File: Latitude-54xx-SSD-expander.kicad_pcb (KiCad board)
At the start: 4 copper layers, 60 x 112 mm, 24 parts, among them J1 Bus_M.2_Socket_M, J2 Bus_M.2_Socket_M, J3 Bus_M.2_Socket_M, J4 qwiic, U1 clockbuffer_9ZXL0651AKLF

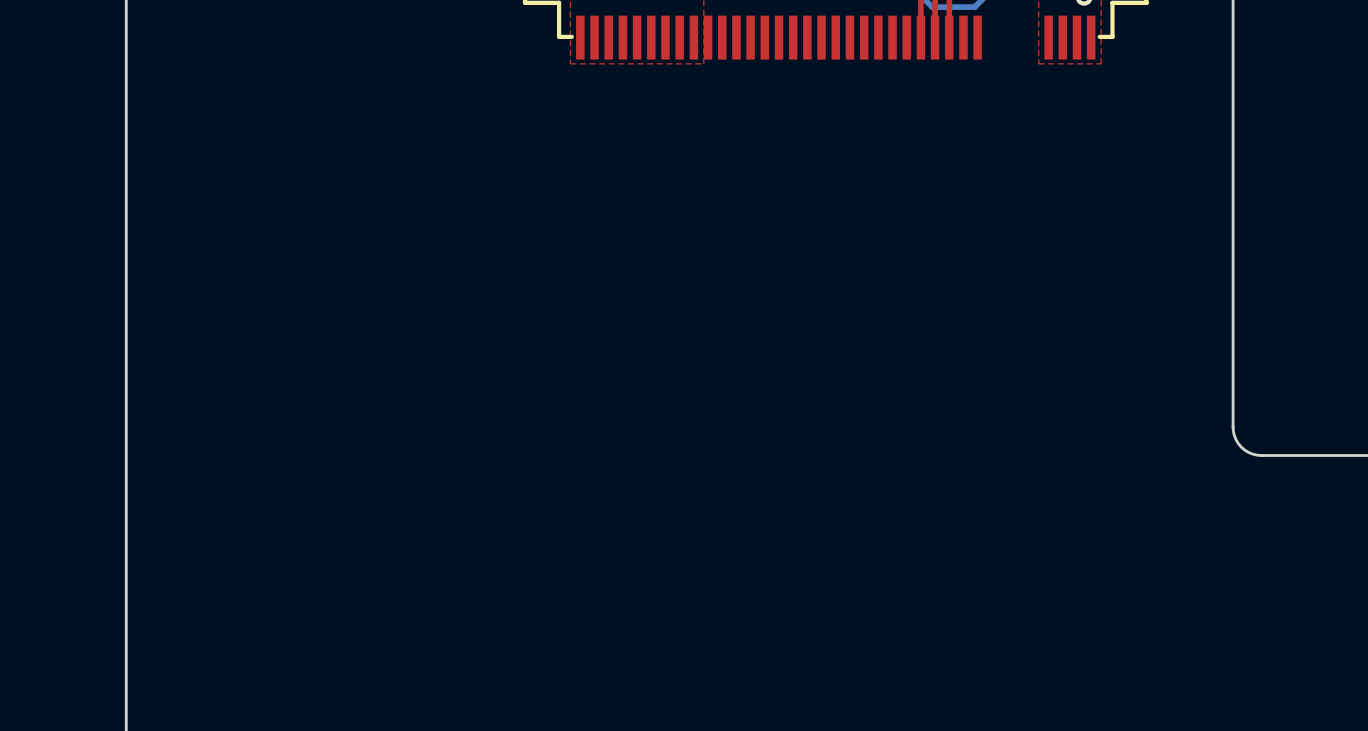
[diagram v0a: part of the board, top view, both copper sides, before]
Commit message: logo concept on the silkscreen
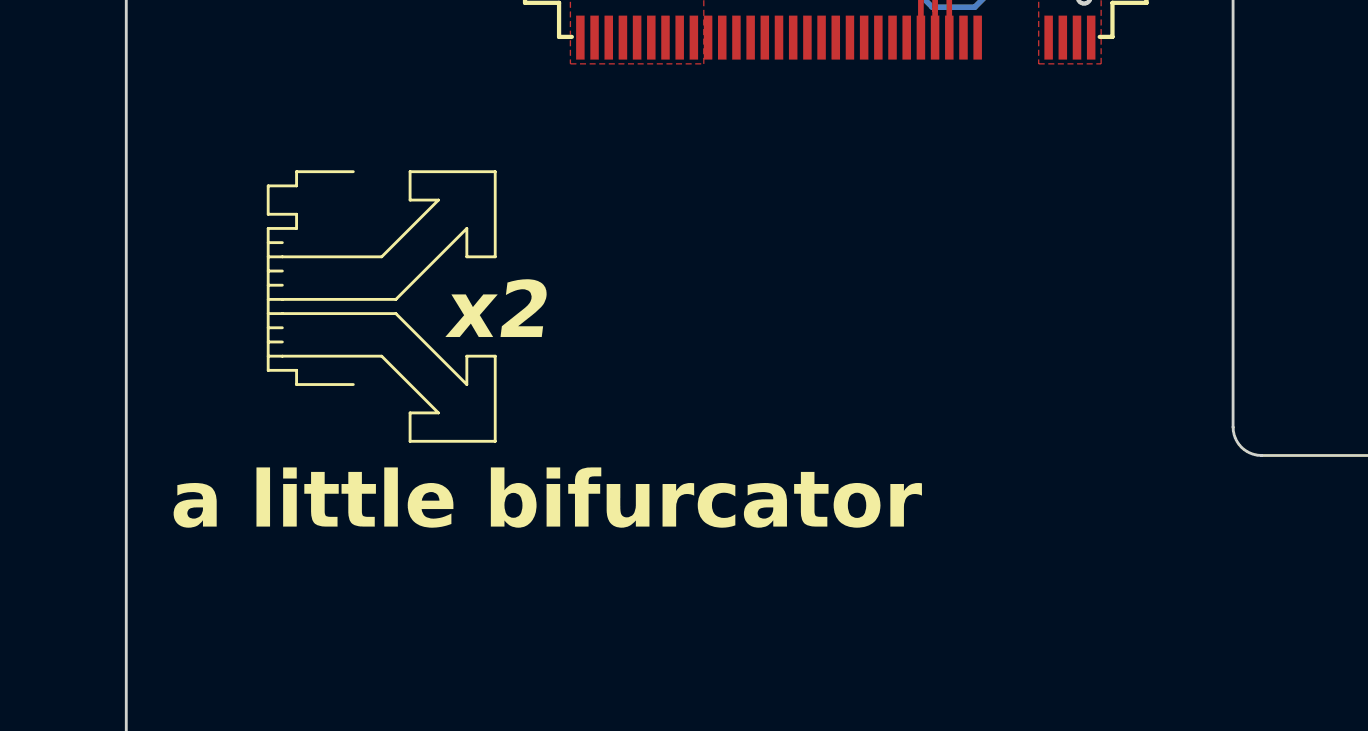
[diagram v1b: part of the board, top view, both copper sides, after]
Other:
- board text added: "a little bifurcator"
- board text added: "x2"

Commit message: Silkscreen adjustments
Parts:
- added G***: LOGO, A-my-stuff:stars, F.Cu at (87.1, 141.1)
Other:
- board text added: "5491 edition"
- board text added: "Buffer SMBus"

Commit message: Added todo list
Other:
- board text added: "TODO: [ ] Properly look into the mounting method to the chassis [ ] Cut off unused PCB area near the end [ ] Come up with a better name/logo"
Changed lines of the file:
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@@
+		)
+	)
+	(gr_text "TODO:\n[ ] Properly look into the mounting method to the chassis\n[ ] Cut off unused PCB area near the end\n[ ] Come up with a better name/logo"
+		(at 146.4 52 0)
+		(layer "User.1")
+		(effects
+			(font
+				(size 1 1)
+				(thickness 0.15)
+			)
+			(justify left bottom)
 		)
 	)

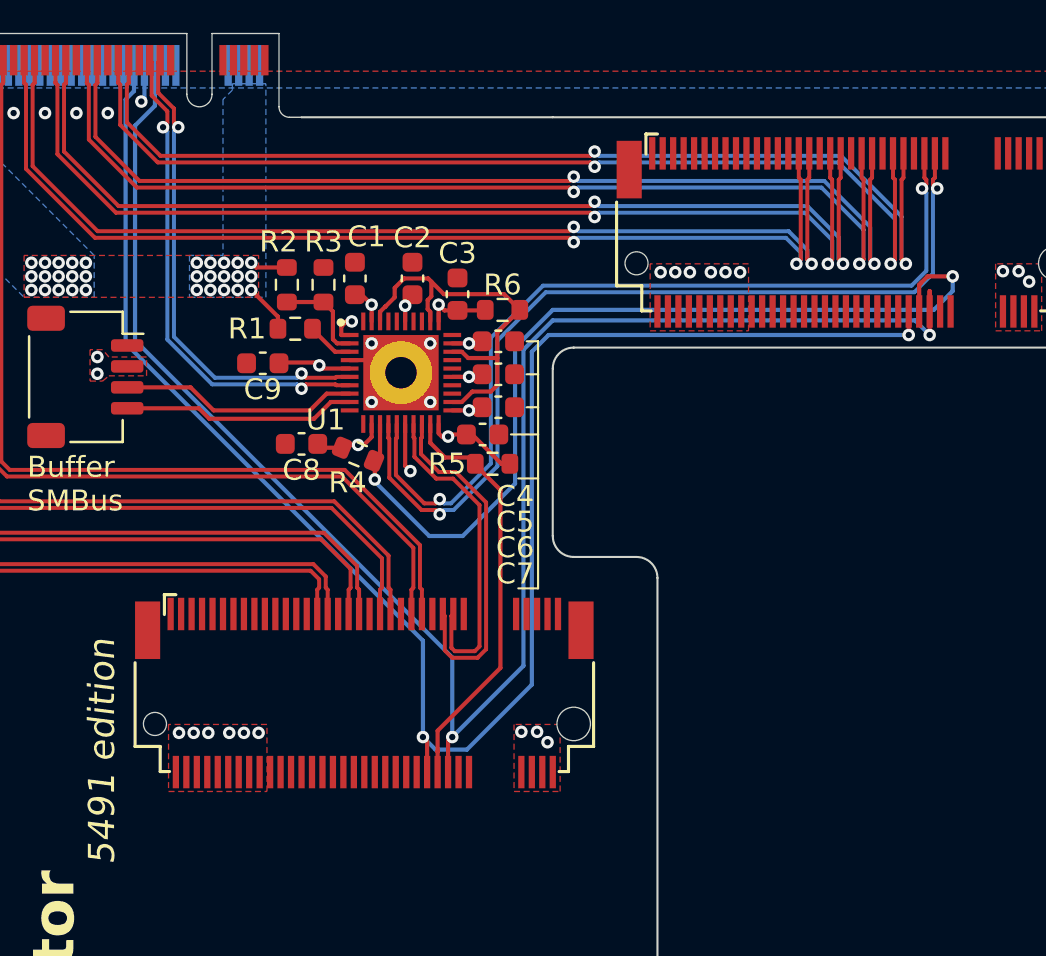
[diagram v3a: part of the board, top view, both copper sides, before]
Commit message: Added capacitors for m.2 slots and ground vias for pcie
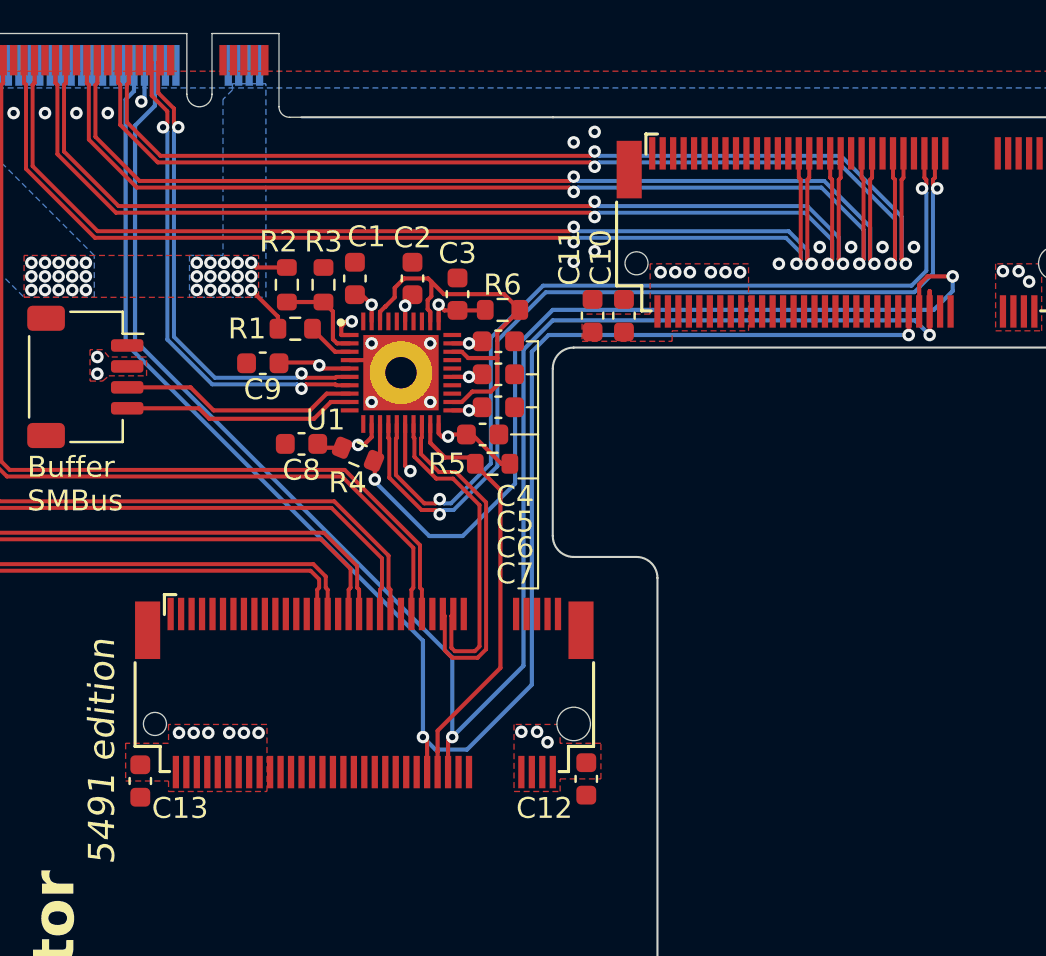
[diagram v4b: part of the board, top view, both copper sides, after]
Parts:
- added C10: 100nF, Capacitor_SMD:C_0603_1608Metric, F.Cu at (116.4, 53.5)
- added C11: 10uF, Capacitor_SMD:C_0603_1608Metric, F.Cu at (114.9, 53.5)
- added C12: 100nF, Capacitor_SMD:C_0603_1608Metric, F.Cu at (114.6, 75.6)
- added C13: 10uF, Capacitor_SMD:C_0603_1608Metric, F.Cu at (93.3, 75.7)
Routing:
- net GND: vias 12 -> 21
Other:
- board text added: "TODO: [ ] Properly look into the mounting method to the chassis [ ] Cut off unused PCB area near the end [ ] Come up with a better name/logo [?] diffpair ground vias [x] M.2 slot capacitors"
- board text removed: "TODO: [ ] Properly look into the mounting method to the chassis [ ] Cut off unused PCB area near the end [ ] Come up with a better name/logo"

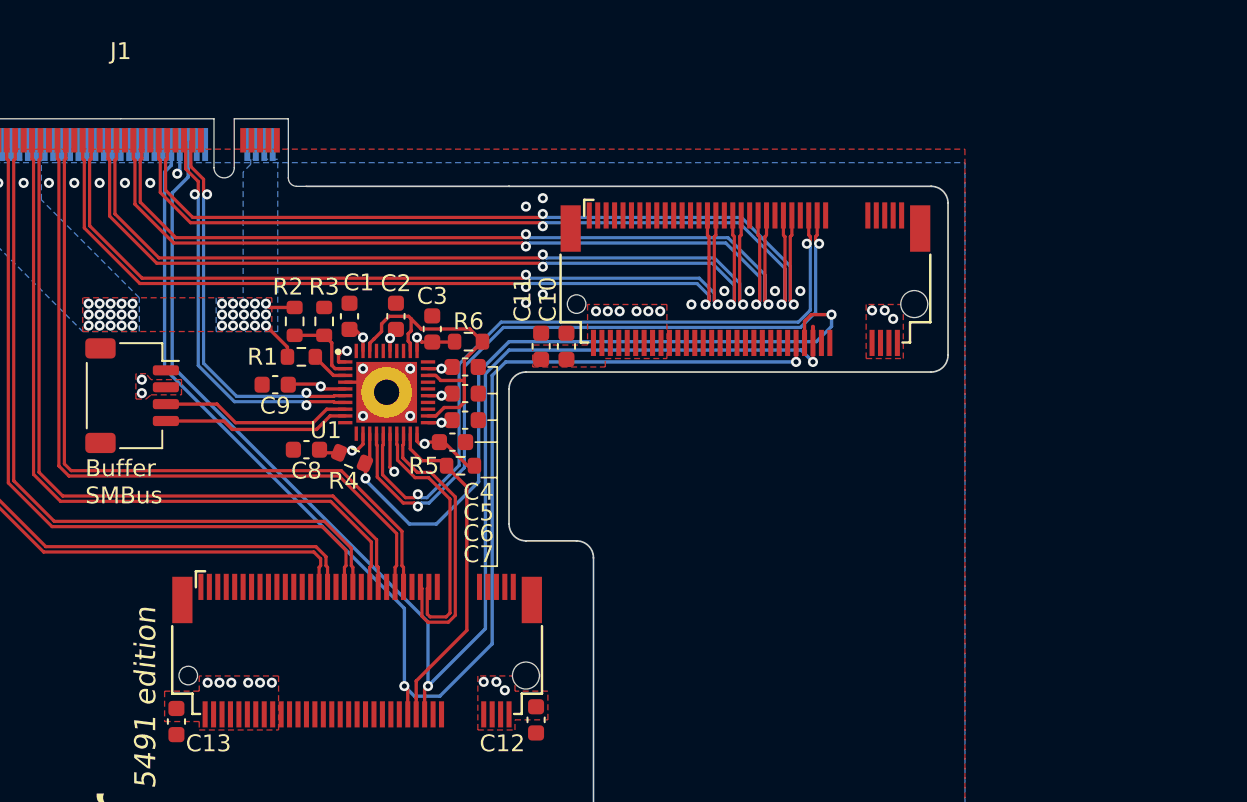
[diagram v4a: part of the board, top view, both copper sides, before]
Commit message: fixed m.2 slot refdes
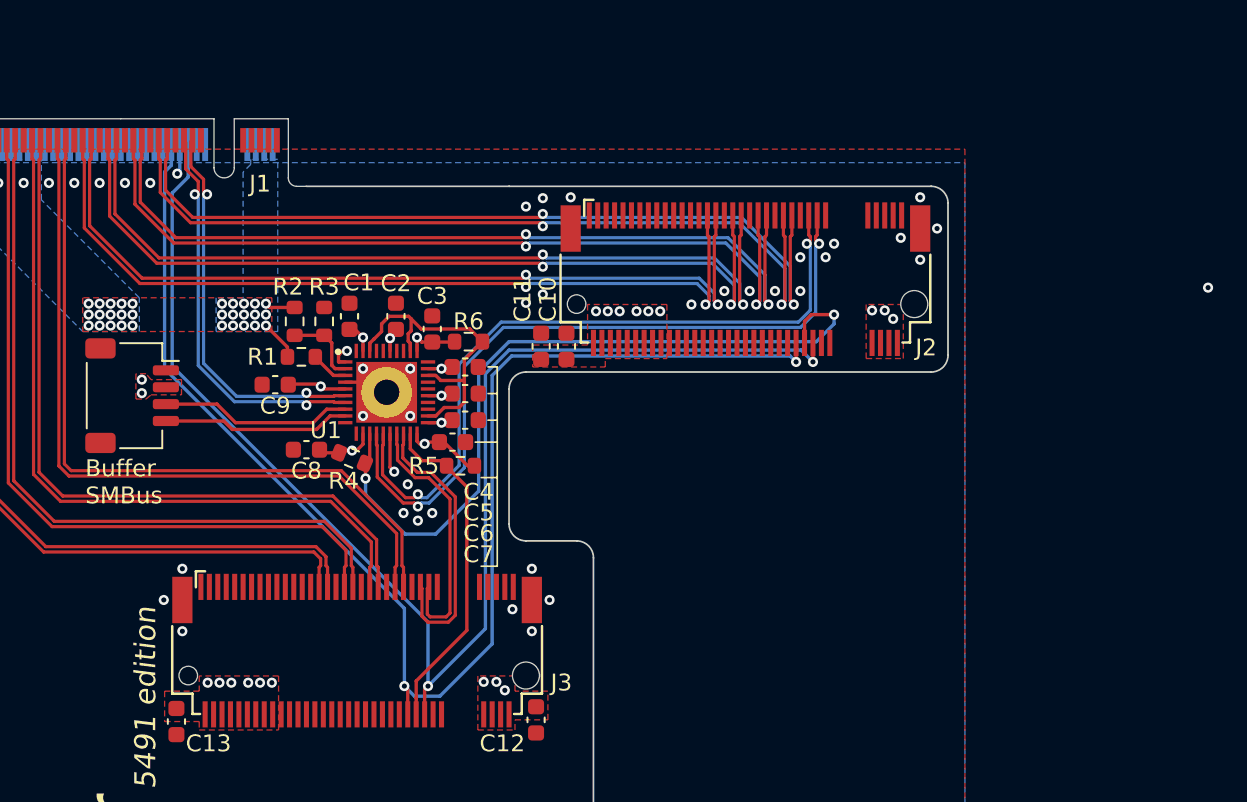
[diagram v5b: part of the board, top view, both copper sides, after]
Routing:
- net PEWAKE#: track 83.8 -> 81.8 mm
- net SSD1_CLKREQ#: track 44.0 -> 45.5 mm
- net GND: vias 21 -> 40
- net (no net): vias 0 -> 1
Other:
- board text added: "TODO: [ ] Properly look into the mounting method to the chassis [ ] Cut off unused PCB area near the end [ ] Come up with a better name/logo [?] diffpair ground vias [x] M.2 slot capacitors [ ] remove ground around diffpairs? [ ] more ground vias"
- board text removed: "TODO: [ ] Properly look into the mounting method to the chassis [ ] Cut off unused PCB area near the end [ ] Come up with a better name/logo [?] diffpair ground vias [x] M.2 slot capacitors"

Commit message: Added activity leds
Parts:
- added D1: LED, Diode_SMD:D_0603_1608Metric, F.Cu at (121.1, 56.6)
- added D2: LED, Diode_SMD:D_0603_1608Metric, F.Cu at (120.1, 73.6)
- added R7: 5K1, Resistor_SMD:R_0603_1608Metric, F.Cu at (125.5, 56.6)
- added R8: 5K1, Resistor_SMD:R_0603_1608Metric, F.Cu at (124.5, 73.5)
- moved C10 1.61 mm to (115.3, 52.3)
- moved C11 1.61 mm to (113.8, 52.3)
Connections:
- J2 pad 10: unconnected-(J2-DAS/~{DSS}/~{LED1}-Pad10) -> Net-(D1-K)
- J3 pad 10: unconnected-(J3-DAS/~{DSS}/~{LED1}-Pad10) -> Net-(D2-K)
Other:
- board text added: "v1 by WifiCable"

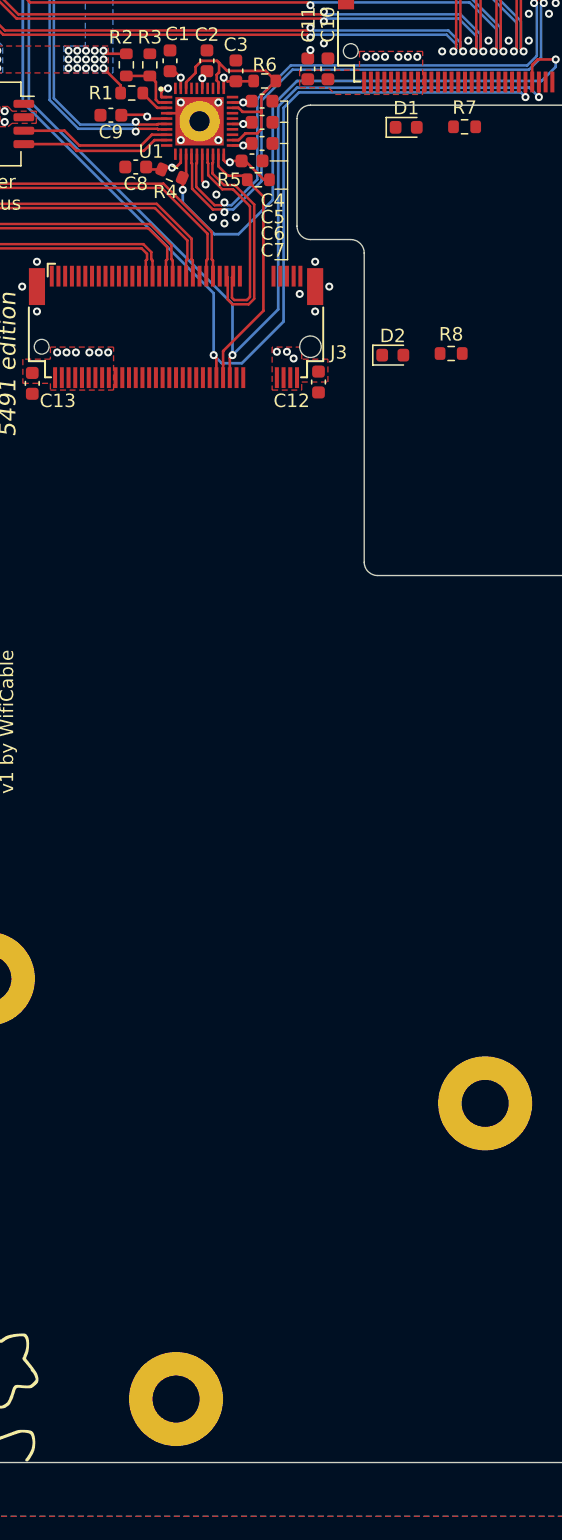
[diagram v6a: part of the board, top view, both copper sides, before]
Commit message: led placement and traces
this was supposed to already be there???
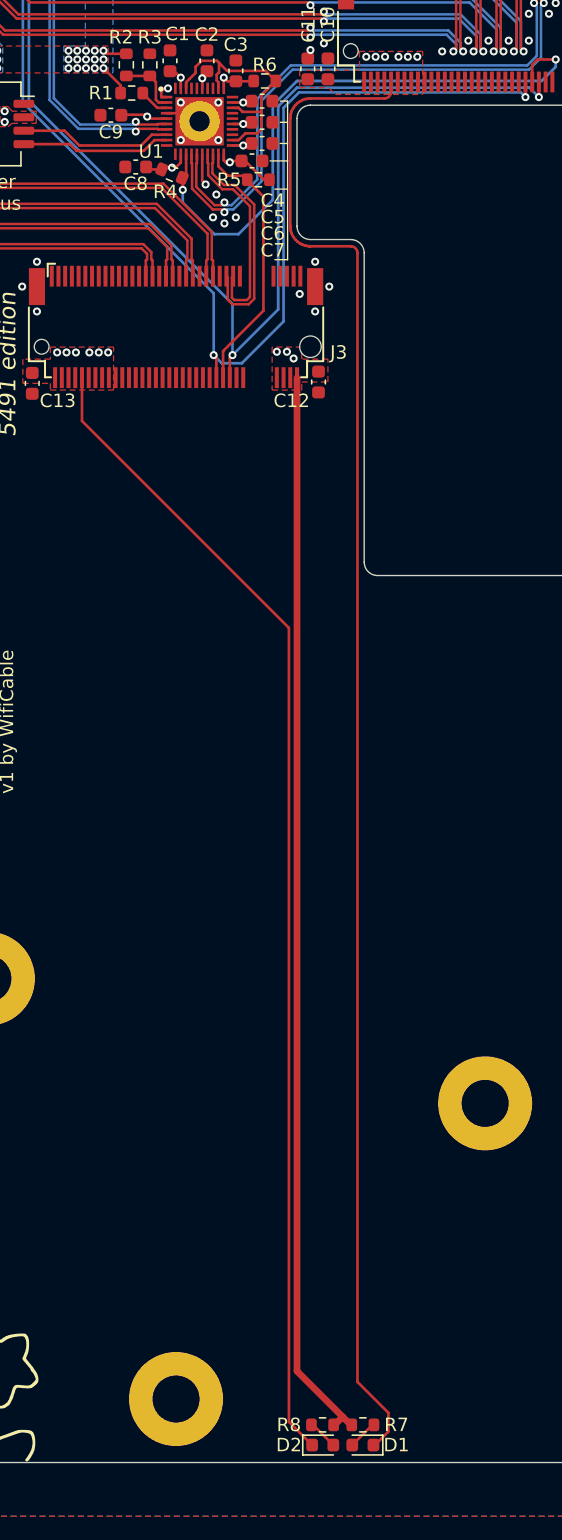
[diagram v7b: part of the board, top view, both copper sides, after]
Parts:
- moved D1 98.1 mm to (117.9, 154.7), turned to 180 degrees
- moved R7 96.9 mm to (117.9, 153.2), turned to 180 degrees
- moved D2 81.3 mm to (114.9, 154.7)
- moved R8 80.3 mm to (114.9, 153.2)
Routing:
- net Net-(D1-K): track 0.00 -> 113.7 mm
- net Net-(D2-K): track 0.00 -> 86.5 mm
- net +3.3V: track 30.3 -> 110.9 mm
- net Net-(D2-A): track 0.00 -> 2.25 mm
- net Net-(D1-A): track 0.00 -> 2.23 mm
